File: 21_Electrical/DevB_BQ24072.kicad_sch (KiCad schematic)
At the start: 99 parts, among them J1 USB4135-GF-A_REVA, J3 SWD1, J8 Conn_01x07_Pin, SW1 BTN, SW2 BOOT0, T1 SWEB_8094, T2 SWEB_8094, T3 SWEB_8094, T4 SWEB_8094, U1 BQ24072RGT, U2 STM32F030F4Px

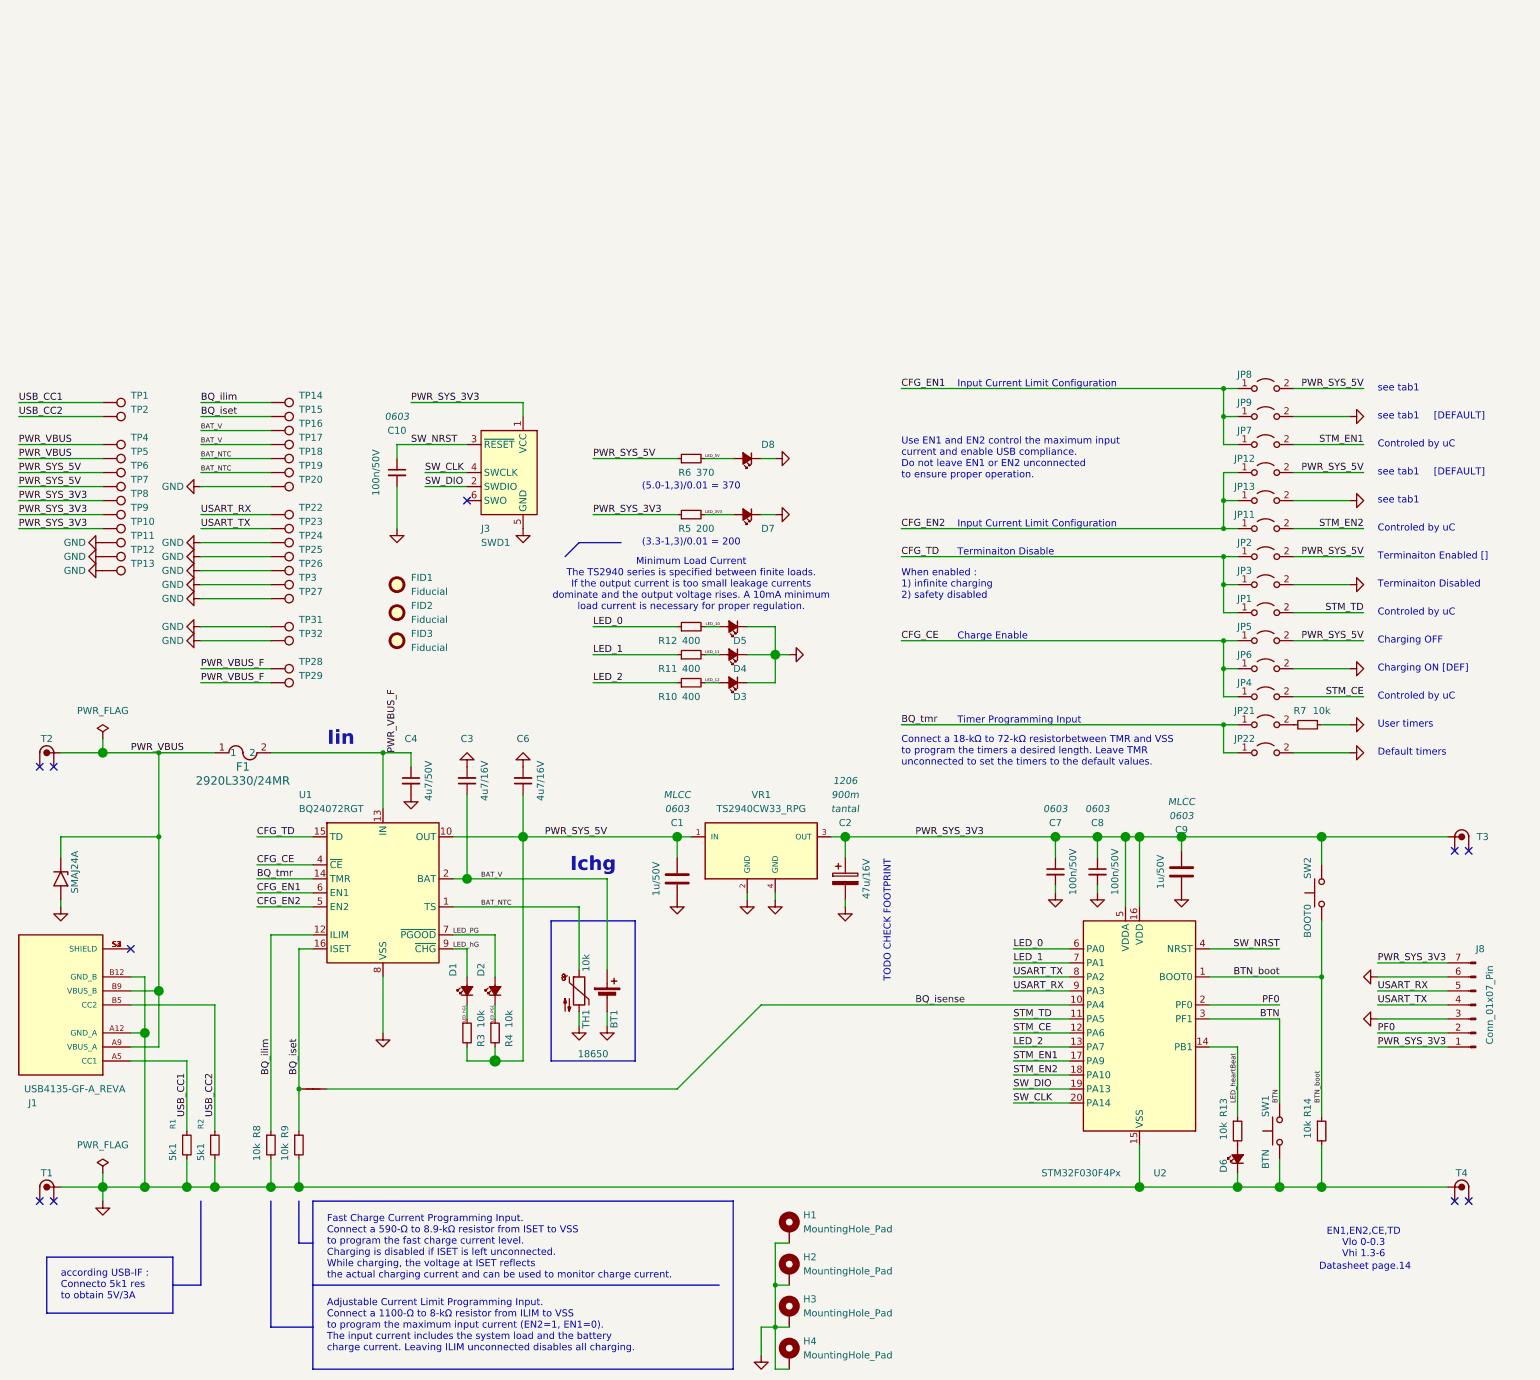
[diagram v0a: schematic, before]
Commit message: PCB added SWD programateor connectors, README.MD update
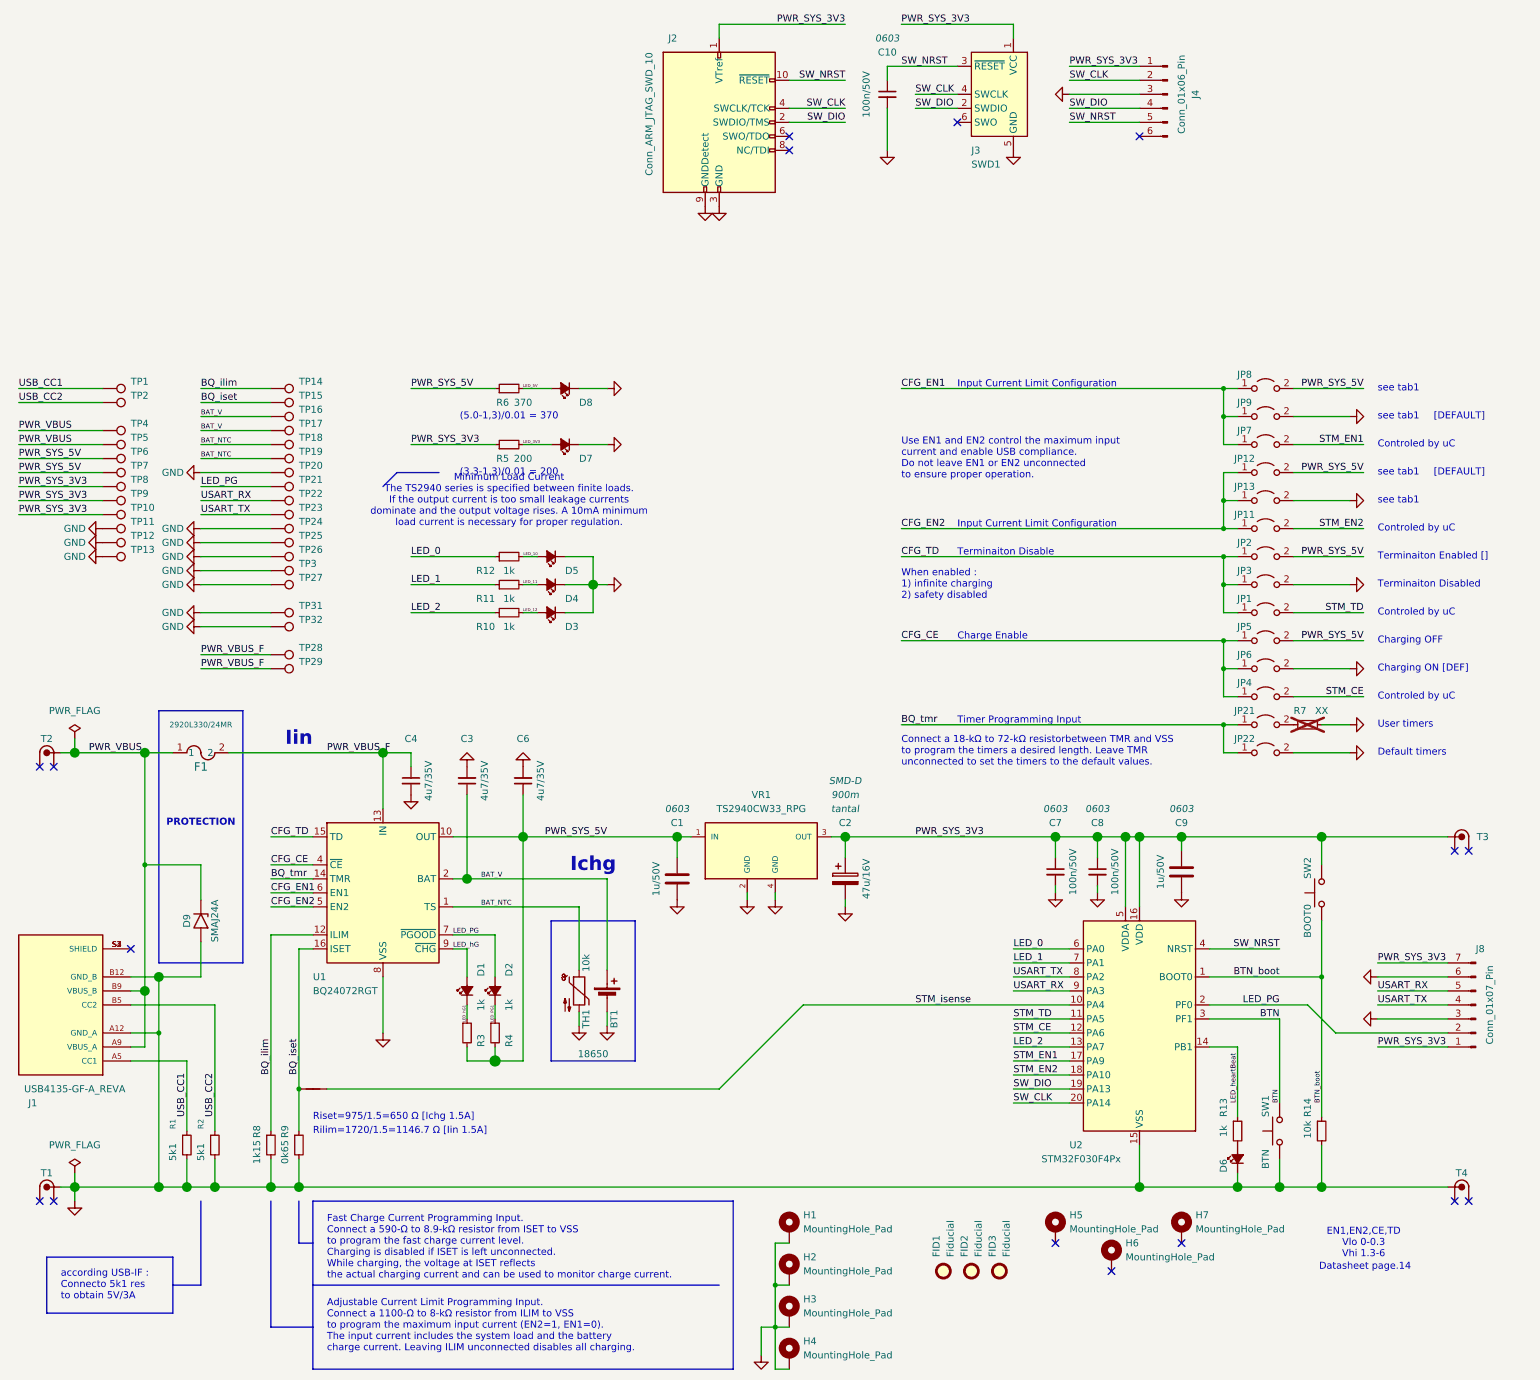
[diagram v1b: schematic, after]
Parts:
- added H5, H6, H7: MountingHole_Pad, MountingHole:ToolingHole_1.152mm, symbol Mechanical:MountingHole_Pad
- added J2: Conn_ARM_JTAG_SWD_10, Connector_PinHeader_1.27mm:PinHeader_2x05_P1.27mm_Vertical_SMD, symbol Connector:Conn_ARM_JTAG_SWD_10
- added J4: Conn_01x06_Pin, Connector_Harwin:Harwin_M20-89006xx_1x06_P2.54mm_Horizontal, symbol Connector:Conn_01x06_Pin
- added TP21: PG, TestPoint:TestPoint_Pad_D1.0mm, symbol Connector:TestPoint
- C2: footprint Capacitor_Tantalum_SMD:CP_EIA-7132-28_AVX-C -> Capacitor_Tantalum_SMD:CP_EIA-7343-31_Kemet-D_HandSolder; Packgate 1206 -> SMD-D
- C3, C6: value 4u7/16V -> 4u7/35V
- C4: value 4u7/50V -> 4u7/35V
- R10, R11, R12: value 400 -> 1k
- R13, R3, R4: value 10k -> 1k
- R7: value 10k -> XX; now not fitted; now left out of the parts list
- R8: value 10k -> 1k15
- R9: value 10k -> 0k65
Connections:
- net PF0 is gone; now on net LED_PG: J8.2 (Pin_2), U2.2 (PF0)
- net GND: now also J2.3 (GND), J2.5 (GND), J2.9 (GNDDetect), J4.3 (Pin_3)
- net LED_PG: now also TP21.1
- net PWR_SYS_3V3: now also J2.1 (VTref), J4.1 (Pin_1)
- net SW_CLK: now also J2.4 (SWCLK/TCK), J4.2 (Pin_2)
- net SW_DIO: now also J2.2 (SWDIO/TMS), J4.4 (Pin_4)
- net SW_NRST: now also J2.10 (~{RESET}), J4.5 (Pin_5)
- net BQ_isense renamed STM_isense
- no-connect marks 10 -> 16
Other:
- note added: "PROTECTION"
- note added: "Rilim=1720/1.5=1146.7 Ω [Iin 1.5A]"
- note added: "Riset=975/1.5=650 Ω [Ichg 1.5A]"
- note removed: "TODO CHECK FOOTPRINT"
- moved on the sheet: C10, D3, D4, D5, D7, D8, F1, FID1, FID2, FID3, J3, R10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
